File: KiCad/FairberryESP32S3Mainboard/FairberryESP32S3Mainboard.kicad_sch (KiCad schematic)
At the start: 31 parts, among them J1 BBQ10KBD, J2 Micro_SD_Card, J3 JST-PH 2-pin (battery), J4 Speaker 2-pin, J5 Trackball (ICSH044A), J6 USB (SIMPLIFIED, see note), U1 ESP32-S3-WROOM-1, U2 MCP73831T-2ACI/OT, U3 MCP1700T-3302E/TT (3.3V, see 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, U4 MAX98357A, U5 ICS-43434, U6 MCP100T-300D/TT (3.0V, see no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

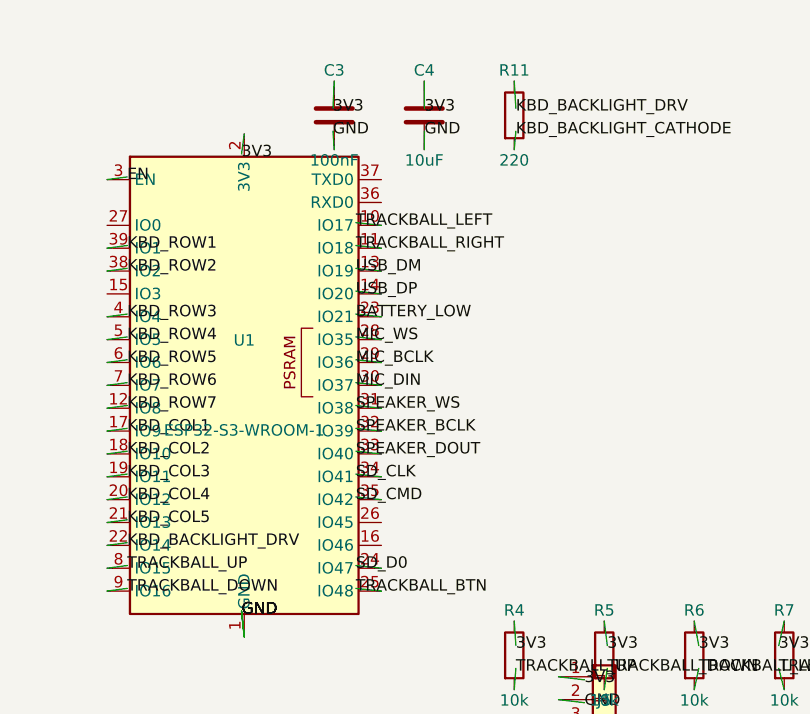
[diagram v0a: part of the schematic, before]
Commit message: Spec ESP32-S3-WROOM-1-N16R8 (octal PSRAM) and move mic I2S off GPIO35-37
Settled the "which ESP32-S3 module" question by verifying real specs for
several candidate boards (XIAO ESP32-S3, Unexpected Maker ProS3/FeatherS3,
ESP32-S3-DevKitC-1) rather than guessing pin counts. None of the small
integrated modules combine enough free GPIO for this design's ~28-pin
budget with onboard USB-C+LiPo charging -- that combination doesn't
really exist at this size class. Since this is a custom PCB, the better
move is placing the bare ESP32-S3-WROOM-1 module directly (already done)
and picking a specific SKU for the BOM rather than leaving flash/PSRAM
unspecified.

Picked -N16R8 (16MB flash, 8MB octal PSRAM) for real RAM headroom on
audio buffers, the web dashboard, and WiFi/TLS. Verified this has one
consequence: on any octal-PSRAM WROOM-1 SKU, GPIO35/36/37 are wired
internally to the in-package PSRAM and aren't usable as GPIO, even
though the generic KiCad symbol still draws them as ordinary pins. Mic
I2S (previously on 35/36/37) moves to GPIO43/44 (the module's UART0
pins, free because this board's console runs over native USB, not
UART0) and GPIO46 (a strapping pin, safe for MIC_DIN since it's an
input and the mic doesn't drive it during a bootloader-mode reset).

Updated boards.h, the hardware doc's pin table, and regenerated+
reverified the KiCad schematic (same 44 real nets, netlist re-checked
via kicad-cli -- still zero dangling nets, only the expected no-connects).

Co-Authored-By: Claude Sonnet 5 <noreply@anthropic.com>
Claude-Session: https://claude.ai/code/session_01APKxwwuAyE76aszQ6arZJ9
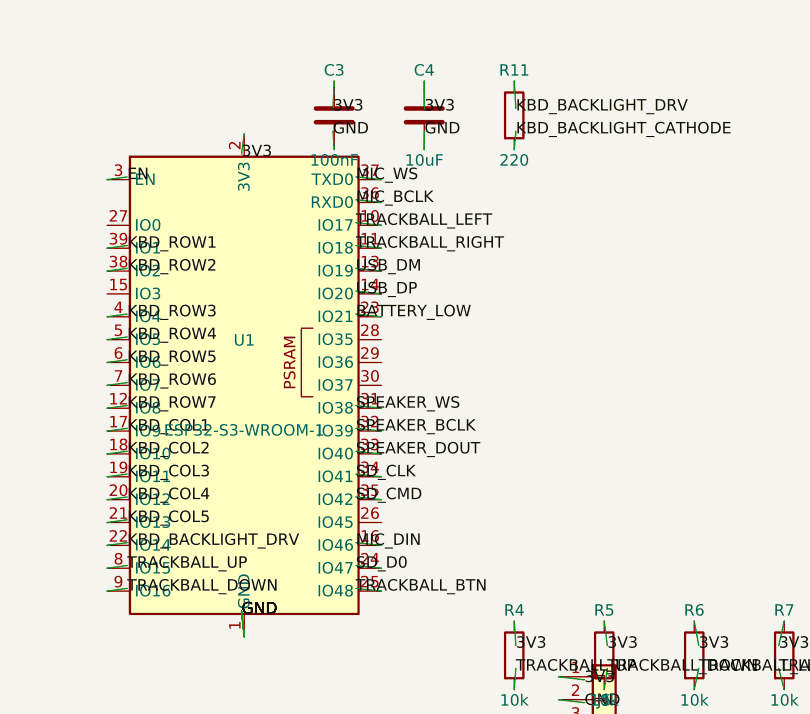
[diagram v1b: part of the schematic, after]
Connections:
- net MIC_BCLK: now also U1.36 (RXD0); no longer U1.29 (IO36)
- net MIC_DIN: now also U1.16 (IO46); no longer U1.30 (IO37)
- net MIC_WS: now also U1.37 (TXD0); no longer U1.28 (IO35)

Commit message: Import the schematic netlist into a new .kicad_pcb
kicad-cli 7's pcb subcommand only has export, not netlist import, and
the GUI's "Update PCB from Schematic" dialog isn't scriptable, so this
does that step directly against the pcbnew Python API
(generator/build_pcb.py): load each component's real footprint, place
it on an unrouted grid, and wire every pad to its net by pad number.

Caught and fixed two real bugs this surfaced, both invisible at the
schematic level since a Footprint property string is just text there,
never validated against real files:
 - the microSD footprint reference (Connector_Card:Conn_01x08_MicroSD_Card)
   was a guessed name that doesn't exist; replaced with a real, verified
   part (microSD_HC_Wuerth_693072010801) whose pad numbering was checked
   pad-by-pad against the symbol's pins, including the 4 physical shield
   pads that share pad number 9 against the symbol's single SHIELD pin
 - the custom keyboard connector's footprint was referenced under an
   invented "Fairberry:" library instead of the real
   "Connectors_Hirose_extra:" one it actually lives in

Verified the result: 31 footprints, 44 nets, zero dangling nets, and
every unconnected pad cross-checked against the already-known list of
intentional no-connects (strapping pins, PSRAM-reserved pins, MAX98357A
NC pins, the keyboard's unused mic pin, plus a handful of
footprint-only mechanical/thermal pads that were never part of the
schematic symbols to begin with). Loads and exports cleanly via
kicad-cli pcb export svg.

No board outline, placement optimization, or routing yet -- this is
the netlist-import step only, both documented as the current state in
the README.

Co-Authored-By: Claude Sonnet 5 <noreply@anthropic.com>
Claude-Session: https://claude.ai/code/session_01APKxwwuAyE76aszQ6arZJ9
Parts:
- J1: footprint Fairberry:BM14B(0.8)-24DS-0.4V(53) -> Connectors_Hirose_extra:BM14B(0.8)-24DS-0.4V(53)
- J2: footprint Connector_Card:Conn_01x08_MicroSD_Card -> Connector_Card:microSD_HC_Wuerth_693072010801
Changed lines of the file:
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@@
     (instances
       (project "FairberryESP32S3Mainboard"
-        (path "/4ce67522-b173-4328-9fb3-923e24df3e17"
+        (path "/dbe6a679-fdac-4e07-8e2f-15233108e7bb"
           (reference "U1") (unit 1)
         )
@@
     (instances
       (project "FairberryESP32S3Mainboard"
-        (path "/4ce67522-b173-4328-9fb3-923e24df3e17"
+        (path "/dbe6a679-fdac-4e07-8e2f-15233108e7bb"
           (reference "U2") (unit 1)
         )
@@
     (instances
       (project "FairberryESP32S3Mainboard"
-        (path "/4ce67522-b173-4328-9fb3-923e24df3e17"
+        (path "/dbe6a679-fdac-4e07-8e2f-15233108e7bb"
           (reference "U3") (unit 1)
         )
@@
     (instances
       (project "FairberryESP32S3Mainboard"
-        (path "/4ce67522-b173-4328-9fb3-923e24df3e17"
+        (path "/dbe6a679-fdac-4e07-8e2f-15233108e7bb"
           (reference "U4") (unit 1)
         )
@@
     (instances
       (project "FairberryESP32S3Mainboard"
-        (path "/4ce67522-b173-4328-9fb3-923e24df3e17"
+        (path "/dbe6a679-fdac-4e07-8e2f-15233108e7bb"
           (reference "U6") (unit 1)
         )
@@
     (instances
       (project "FairberryESP32S3Mainboard"
-        (path "/4ce67522-b173-4328-9fb3-923e24df3e17"
+        (path "/dbe6a679-fdac-4e07-8e2f-15233108e7bb"
           (reference "U5") (unit 1)
         )
@@
     (property "Reference" "J1" (at 40 135 0) (effects (font (size 1.27 1.27))))
     (property "Value" "BBQ10KBD" (at 40 145 0) (effects (font (size 1.27 1.27))))
-    (property "Footprint" "Fairberry:BM14B(0.8)-24DS-0.4V(53)" (at 40 140 0) (effects (font (size 1.27 1.27)) hide))
+    (property "Footprint" "Connectors_Hirose_extra:BM14B(0.8)-24DS-0.4V(53)" (at 40 140 0) (effects (font (size 1.27 1.27)) hide))
     (property "Datasheet" "" (at 40 140 0) (effects (font (size 1.27 1.27)) hide))
     (pin "1")
@@
     (instances
       (project "FairberryESP32S3Mainboard"
-        (path "/4ce67522-b173-4328-9fb3-923e24df3e17"
+        (path "/dbe6a679-fdac-4e07-8e2f-15233108e7bb"
           (reference "J1") (unit 1)
         )
@@
     (property "Reference" "J2" (at 280 135 0) (effects (font (size 1.27 1.27))))
     (property "Value" "Micro_SD_Card" (at 280 145 0) (effects (font (size 1.27 1.27))))
-    (property "Footprint" "Connector_Card:Conn_01x08_MicroSD_Card" (at 280 140 0) (effects (font (size 1.27 1.27)) hide))
+    (property "Footprint" "Connector_Card:microSD_HC_Wuerth_693072010801" (at 280 140 0) (effects (font (size 1.27 1.27)) hide))
     (property "Datasheet" "" (at 280 140 0) (effects (font (size 1.27 1.27)) hide))
     (pin "1")
@@
     (instances
       (project "FairberryESP32S3Mainboard"
-        (path "/4ce67522-b173-4328-9fb3-923e24df3e17"
+        (path "/dbe6a679-fdac-4e07-8e2f-15233108e7bb"
           (reference "J2") (unit 1)
         )
@@
     (instances
       (project "FairberryESP32S3Mainboard"
-        (path "/4ce67522-b173-4328-9fb3-923e24df3e17"
+        (path "/dbe6a679-fdac-4e07-8e2f-15233108e7bb"
           (reference "J3") (unit 1)
         )
@@
     (instances
       (project "FairberryESP32S3Mainboard"
-        (path "/4ce67522-b173-4328-9fb3-923e24df3e17"
+        (path "/dbe6a679-fdac-4e07-8e2f-15233108e7bb"
           (reference "J4") (unit 1)
         )
@@
     (instances
       (project "FairberryESP32S3Mainboard"
-        (path "/4ce67522-b173-4328-9fb3-923e24df3e17"
+        (path "/dbe6a679-fdac-4e07-8e2f-15233108e7bb"
           (reference "J5") (unit 1)
         )
@@
     (instances
       (project "FairberryESP32S3Mainboard"
-        (path "/4ce67522-b173-4328-9fb3-923e24df3e17"
+        (path "/dbe6a679-fdac-4e07-8e2f-15233108e7bb"
           (reference "J6") (unit 1)
         )
@@
     (instances
       (project "FairberryESP32S3Mainboard"
-        (path "/4ce67522-b173-4328-9fb3-923e24df3e17"
+        (path "/dbe6a679-fdac-4e07-8e2f-15233108e7bb"
           (reference "R1") (unit 1)
         )
@@
     (instances
       (project "FairberryESP32S3Mainboard"
-        (path "/4ce67522-b173-4328-9fb3-923e24df3e17"
+        (path "/dbe6a679-fdac-4e07-8e2f-15233108e7bb"
           (reference "R2") (unit 1)
         )
@@
     (instances
       (project "FairberryESP32S3Mainboard"
-        (path "/4ce67522-b173-4328-9fb3-923e24df3e17"
+        (path "/dbe6a679-fdac-4e07-8e2f-15233108e7bb"
           (reference "R3") (unit 1)
         )
@@
     (instances
       (project "FairberryESP32S3Mainboard"
-        (path "/4ce67522-b173-4328-9fb3-923e24df3e17"
+        (path "/dbe6a679-fdac-4e07-8e2f-15233108e7bb"
           (reference "R4") (unit 1)
         )
@@
     (instances
       (project "FairberryESP32S3Mainboard"
-        (path "/4ce67522-b173-4328-9fb3-923e24df3e17"
+        (path "/dbe6a679-fdac-4e07-8e2f-15233108e7bb"
           (reference "R5") (unit 1)
         )
@@
     (instances
       (project "FairberryESP32S3Mainboard"
-        (path "/4ce67522-b173-4328-9fb3-923e24df3e17"
+        (path "/dbe6a679-fdac-4e07-8e2f-15233108e7bb"
           (reference "R6") (unit 1)
         )
@@
     (instances
       (project "FairberryESP32S3Mainboard"
-        (path "/4ce67522-b173-4328-9fb3-923e24df3e17"
+        (path "/dbe6a679-fdac-4e07-8e2f-15233108e7bb"
           (reference "R7") (unit 1)
         )
@@
     (instances
       (project "FairberryESP32S3Mainboard"
-        (path "/4ce67522-b173-4328-9fb3-923e24df3e17"
+        (path "/dbe6a679-fdac-4e07-8e2f-15233108e7bb"
           (reference "R8") (unit 1)
         )
@@
     (instances
       (project "FairberryESP32S3Mainboard"
-        (path "/4ce67522-b173-4328-9fb3-923e24df3e17"
+        (path "/dbe6a679-fdac-4e07-8e2f-15233108e7bb"
           (reference "R9") (unit 1)
         )
@@
     (instances
       (project "FairberryESP32S3Mainboard"
-        (path "/4ce67522-b173-4328-9fb3-923e24df3e17"
+        (path "/dbe6a679-fdac-4e07-8e2f-15233108e7bb"
           (reference "R10") (unit 1)
         )
@@
     (instances
       (project "FairberryESP32S3Mainboard"
-        (path "/4ce67522-b173-4328-9fb3-923e24df3e17"
+        (path "/dbe6a679-fdac-4e07-8e2f-15233108e7bb"
           (reference "R11") (unit 1)
         )
@@
     (instances
       (project "FairberryESP32S3Mainboard"
-        (path "/4ce67522-b173-4328-9fb3-923e24df3e17"
+        (path "/dbe6a679-fdac-4e07-8e2f-15233108e7bb"
           (reference "R12") (unit 1)
         )
@@
     (instances
       (project "FairberryESP32S3Mainboard"
-        (path "/4ce67522-b173-4328-9fb3-923e24df3e17"
+        (path "/dbe6a679-fdac-4e07-8e2f-15233108e7bb"
           (reference "C1") (unit 1)
         )
@@
     (instances
       (project "FairberryESP32S3Mainboard"
-        (path "/4ce67522-b173-4328-9fb3-923e24df3e17"
+        (path "/dbe6a679-fdac-4e07-8e2f-15233108e7bb"
           (reference "C2") (unit 1)
         )
@@
     (instances
       (project "FairberryESP32S3Mainboard"
-        (path "/4ce67522-b173-4328-9fb3-923e24df3e17"
+        (path "/dbe6a679-fdac-4e07-8e2f-15233108e7bb"
           (reference "C3") (unit 1)
         )
@@
     (instances
       (project "FairberryESP32S3Mainboard"
-        (path "/4ce67522-b173-4328-9fb3-923e24df3e17"
+        (path "/dbe6a679-fdac-4e07-8e2f-15233108e7bb"
           (reference "C4") (unit 1)
         )
@@
     (instances
       (project "FairberryESP32S3Mainboard"
-        (path "/4ce67522-b173-4328-9fb3-923e24df3e17"
+        (path "/dbe6a679-fdac-4e07-8e2f-15233108e7bb"
           (reference "C5") (unit 1)
         )
@@
     (instances
       (project "FairberryESP32S3Mainboard"
-        (path "/4ce67522-b173-4328-9fb3-923e24df3e17"
+        (path "/dbe6a679-fdac-4e07-8e2f-15233108e7bb"
           (reference "C6") (unit 1)
         )
@@
     (instances
       (project "FairberryESP32S3Mainboard"
-        (path "/4ce67522-b173-4328-9fb3-923e24df3e17"
+        (path "/dbe6a679-fdac-4e07-8e2f-15233108e7bb"
           (reference "LED1") (unit 1)
         )
